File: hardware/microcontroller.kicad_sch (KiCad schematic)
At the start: 0 parts

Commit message: Begin MCU
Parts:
- added C501: 4.7uF, symbol Device:C
- added C502, C503, C504, C506, C508: 100nF, symbol Device:C_Small
- added C505: 1uF, symbol Device:C_Small
- added C507: 10nF, symbol Device:C_Small
- added D501: ESD, Diode_SMD:D_SOD-882, symbol carrier-wave:ESDALC6V1-1M2
- added FB501: 600 @ 100Mhz, Inductor_SMD:L_0603_1608Metric, symbol Device:FerriteBead_Small
- added R501: 10k, symbol Device:R_Small_US
- added SW501: RST, symbol Switch:SW_Push
- added U501: STM32G491CCUx, Package_DFN_QFN:QFN-48-1EP_7x7mm_P0.5mm_EP5.6x5.6mm, symbol MCU_ST_STM32G4:STM32G491CCUx
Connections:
- new net +3.3VD: C501.1, C502.1, C503.1, C504.1, C505.1, FB501.1, R501.1, U501.1 (VBAT), U501.23 (VDD), U501.35 (VDD), U501.48 (VDD)
- new net GND: C501.2, C502.2, C503.2, C504.2, C505.2, C506.2, C507.2, C508.2, D501.2 (A), SW501.2, U501.49 (VSS)
- new net VDDA: C506.1, C507.1, FB501.2, U501.21 (VDDA)
- new net ~{NRST}: C508.1, D501.1 (K), R501.2, SW501.1
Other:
- note added: "Ferrite bead low-pass filter isolates VDDA from 3.3VD digital switching noise."
- note added: "One 100nF decoupling capacitor should be placed close to each VDD pin on MCU."
- company: (none) -> Jacob Wigent
- title: (none) -> STM32G4

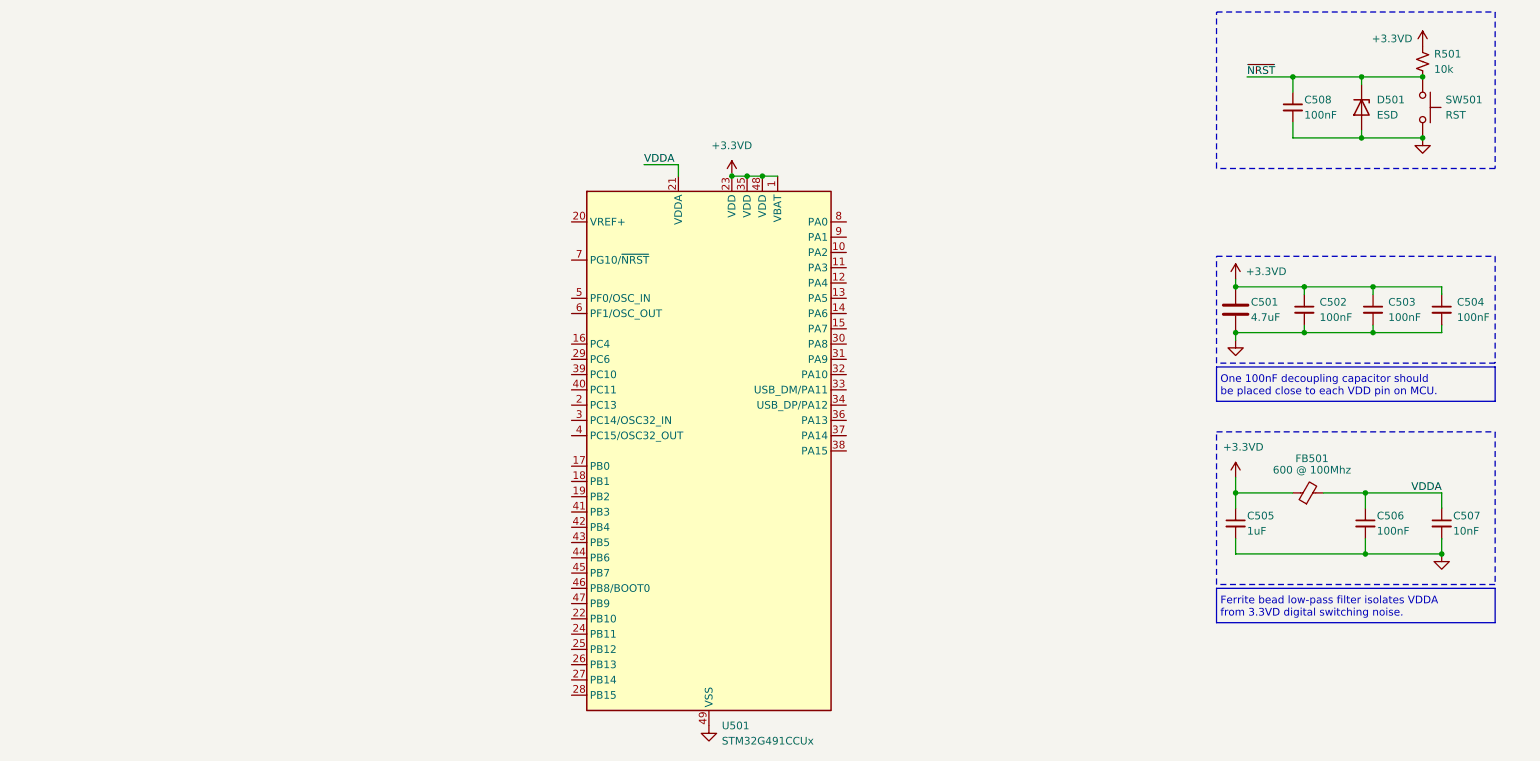
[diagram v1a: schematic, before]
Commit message: Begin MCU pin assignments
Added STM32CubeMX project. Assigned peripheral pins, and began assigning GPIOs.
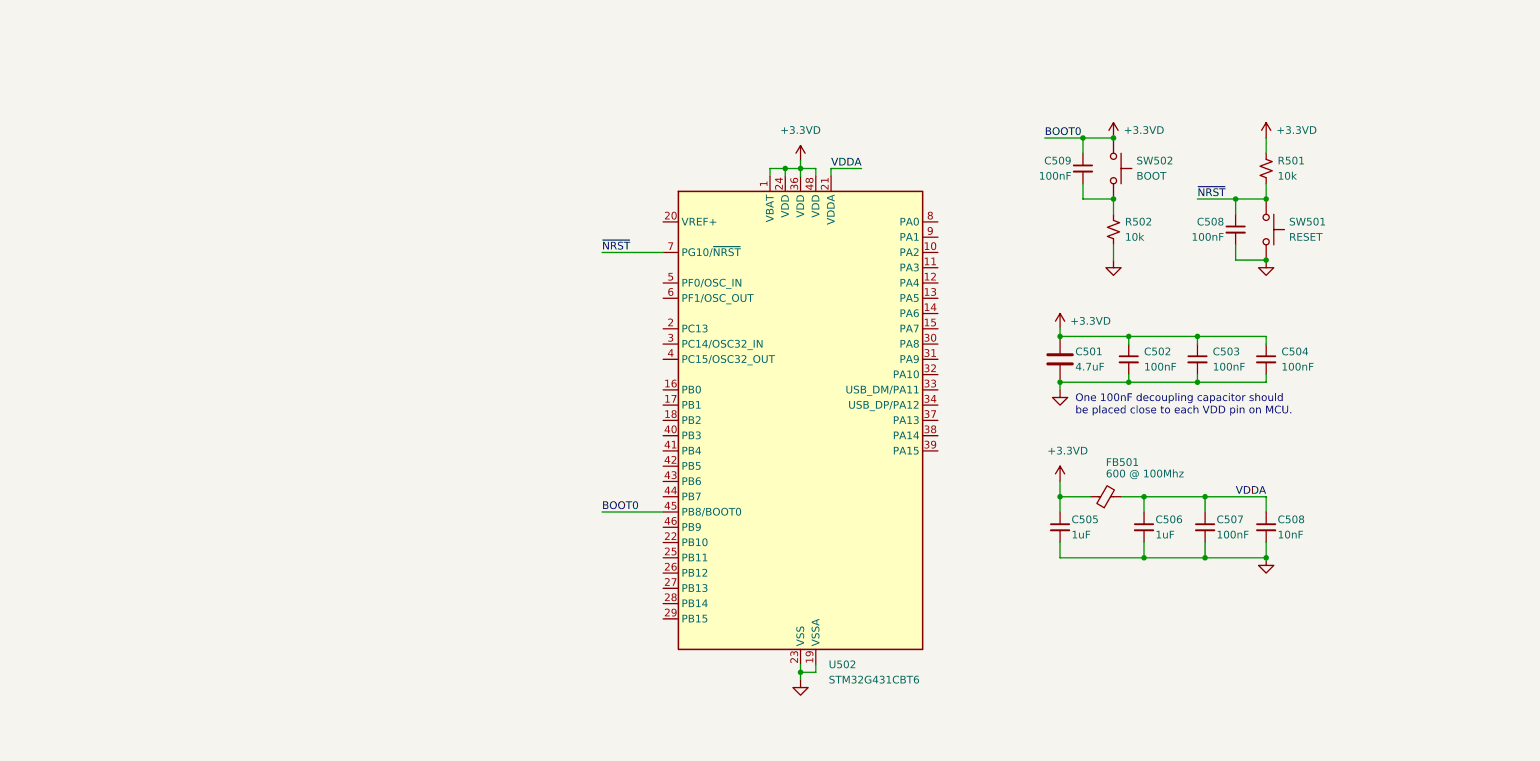
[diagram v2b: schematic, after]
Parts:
- removed D501: ESD, Diode_SMD:D_SOD-882, symbol carrier-wave:ESDALC6V1-1M2
- removed U501: STM32G491CCUx, Package_DFN_QFN:QFN-48-1EP_7x7mm_P0.5mm_EP5.6x5.6mm, symbol MCU_ST_STM32G4:STM32G491CCUx
- added C506: 1uF, symbol Device:C_Small
- added C509: 100nF, symbol Device:C_Small
- added R502: 10k, symbol Device:R_Small_US
- added SW502: BOOT, symbol Switch:SW_Push
- added U502: STM32G431CBT6, Package_QFP:LQFP-48_7x7mm_P0.5mm, symbol MCU_ST_STM32G4:STM32G431CBTx
- SW501: value RST -> RESET
- renumbered C506 to C507, C507 to C508
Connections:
- net +3.3VD: now also C509.1, SW502.1, U502.1 (VBAT), U502.24 (VDD), U502.36 (VDD), U502.45 (PB8/BOOT0), U502.48 (VDD)
- net GND: now also C506.2, R502.2, U502.19 (VSSA), U502.23 (VSS), U502.35 (VSS), U502.47 (VSS)
- net VDDA: now also C506.1, U502.21 (VDDA)
- net ~{NRST}: now also U502.7 (PG10/~{NRST})
- new net: C509.2, R502.1, SW502.2
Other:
- note removed: "Ferrite bead low-pass filter isolates VDDA from 3.3VD digital switching noise."
- moved on the sheet: C501, C502, C503, C504, C505, C507, C508, FB501, R501, SW501

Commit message: Cleanup Sheets
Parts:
- added J501: Conn_ST_STDC14, Connector_PinHeader_1.27mm:PinHeader_2x07_P1.27mm_Vertical_SMD, symbol Connector:Conn_ST_STDC14
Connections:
- new net: J501.5 (GND), J501.7 (GND)
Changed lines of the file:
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@@
+	)
+	(symbol
+		(lib_id "Connector:Conn_ST_STDC14")
+		(at 57.15 71.12 0)
+		(unit 1)
+		(body_style 1)
+		(exclude_from_sim no)
+		(in_bom yes)
+		(on_board yes)
+		(in_pos_files yes)
+		(dnp no)
+		(fields_autoplaced yes)
+		(property "Reference" "J501"
+			(at 45.72 69.8499 0)
+			(show_name no)
+			(do_not_autoplace no)
+			(effects
+				(font
+					(size 1.27 1.27)
+				)
+				(justify right)
+			)
+		)
+		(property "Value" "Conn_ST_STDC14"
+			(at 45.72 72.3899 0)
+			(show_name no)
+			(do_not_autoplace no)
+			(effects
+				(font
+					(size 1.27 1.27)
+				)
+				(justify right)
+			)
+		)
+		(property "Footprint" "Connector_PinHeader_1.27mm:PinHeader_2x07_P1.27mm_Vertical_SMD"
+			(at 57.15 71.12 0)
+			(hide yes)
+			(show_name no)
+			(do_not_autoplace no)
+			(effects
+				(font
+					(size 1.27 1.27)
+				)
+			)
+		)
+		(property "Datasheet" "https://www.st.com/content/ccc/resource/technical/document/user_manual/group1/99/49/91/b6/b2/3a/46/e5/DM00526767/files/DM00526767.pdf/jcr:content/translations/en.DM00526767.pdf"
+			(at 48.26 102.87 90)
+			(hide yes)
+			(show_name no)
+			(do_not_autoplace no)
+			(effects
+				(font
+					(size 1.27 1.27)
+				)
+			)
+		)
+		(property "Description" "ST Debug Connector, standard ARM Cortex-M SWD and JTAG interface plus UART"
+			(at 57.15 71.12 0)
+			(hide yes)
+			(show_name no)
+			(do_not_autoplace no)
+			(effects
+				(font
+					(size 1.27 1.27)
+				)
+			)
+		)
+		(property "Part Number" "FTSH-107-01-F-DV-K-P-TR"
+			(at 57.15 71.12 0)
+			(hide yes)
+			(show_name no)
+			(do_not_autoplace no)
+			(effects
+				(font
+					(size 1.27 1.27)
+				)
+			)
+		)
+		(property "Vendor URL" "https://www.digikey.com/en/products/detail/samtec-inc/FTSH-107-01-F-DV-K-P-TR/6693677"
+			(at 57.15 71.12 0)
+			(hide yes)
+			(show_name no)
+			(do_not_autoplace no)
+			(effects
+				(font
+					(size 1.27 1.27)
+				)
+			)
+		)
+		(pin "7"
+		)
+		(pin "1"
+		)
+		(pin "2"
+		)
+		(pin "3"
+		)
+		(pin "4"
+		)
+		(pin "6"
+		)
+		(pin "5"
+		)
+		(pin "9"
+		)
+		(pin "8"
+		)
+		(pin "10"
+		)
+		(pin "14"
+		)
+		(pin "13"
+		)
+		(pin "11"
+		)
+		(pin "12"
+		)
+		(instances
+			(project "carrier-wave"
+				(path "/dc900721-a2e3-4f11-b4f2-59bb3a47422e/ce2ab052-e0a3-4aff-b808-e261b8e26647"
+					(reference "J501")
+					(unit 1)
+				)
+			)
+		)
 	)
 	(symbol

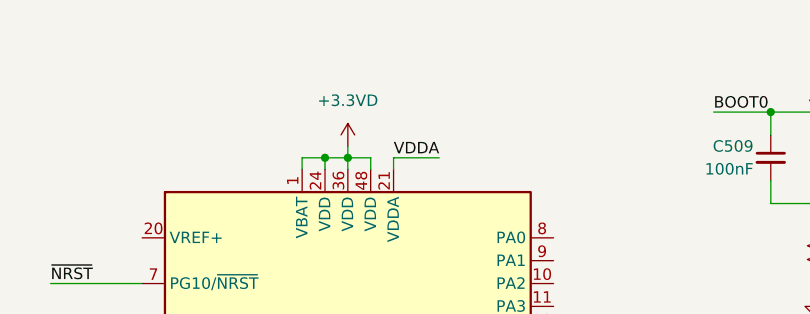
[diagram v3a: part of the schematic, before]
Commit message: Begin VGA impl
Sim and notes on adjusting to 4.5V rails for VGA.
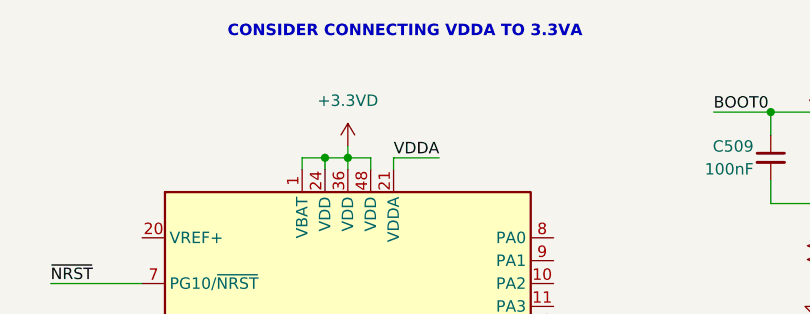
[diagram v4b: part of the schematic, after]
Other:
- note added: "CONSIDER CONNECTING VDDA TO 3.3VA"
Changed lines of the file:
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@@
+		)
+	)
+	(text "CONSIDER CONNECTING VDDA TO 3.3VA"
+		(exclude_from_sim no)
+		(at 165.1 30.48 0)
+		(effects
+			(font
+				(size 1.27 1.27)
+				(thickness 0.254)
+				(bold yes)
+				(color 194 0 0 1)
+			)
 		)
 	)
